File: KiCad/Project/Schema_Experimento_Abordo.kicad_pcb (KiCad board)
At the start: 2 copper layers, 58 x 58 mm, 29 parts, among them SW1 RESET, U1 ESP32-S3-WROOM-1, U2 BME280, U5 Micro_SD, U6 ZC323200, U7 SGP30, U9 AP2112K-3.3

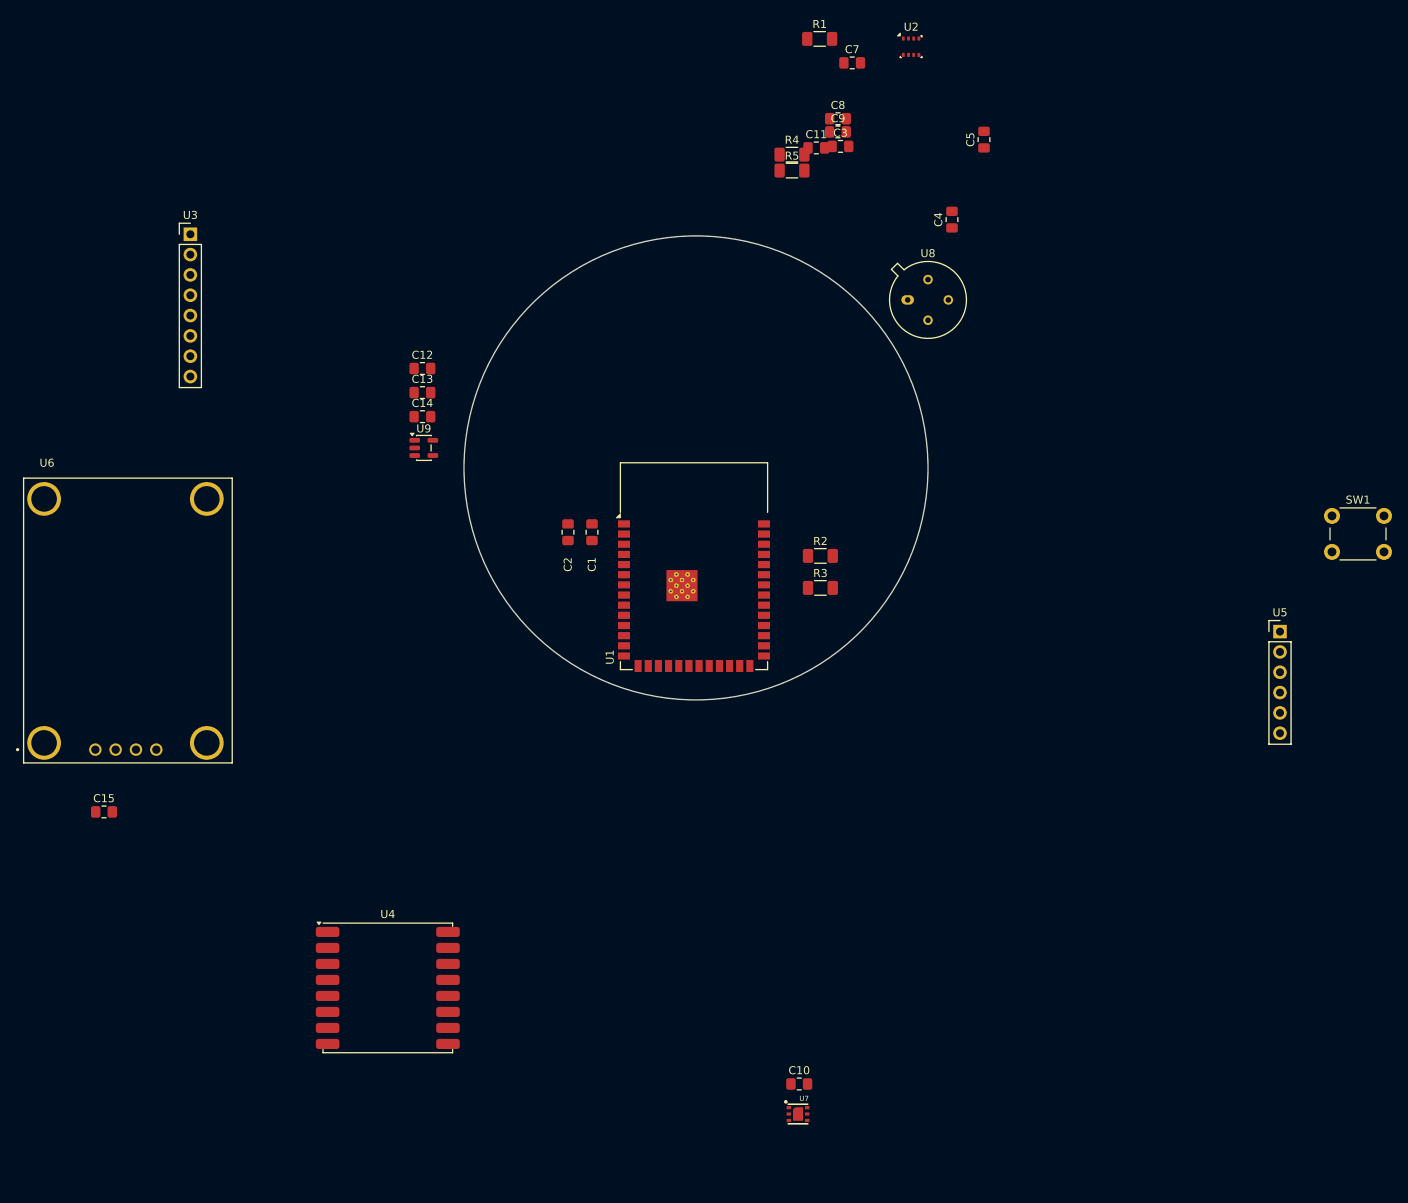
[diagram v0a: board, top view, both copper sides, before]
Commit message: Esquematico limpio y probado. PCB Actualizado. Falta definir si se cambia el U9 por un Buck-boost
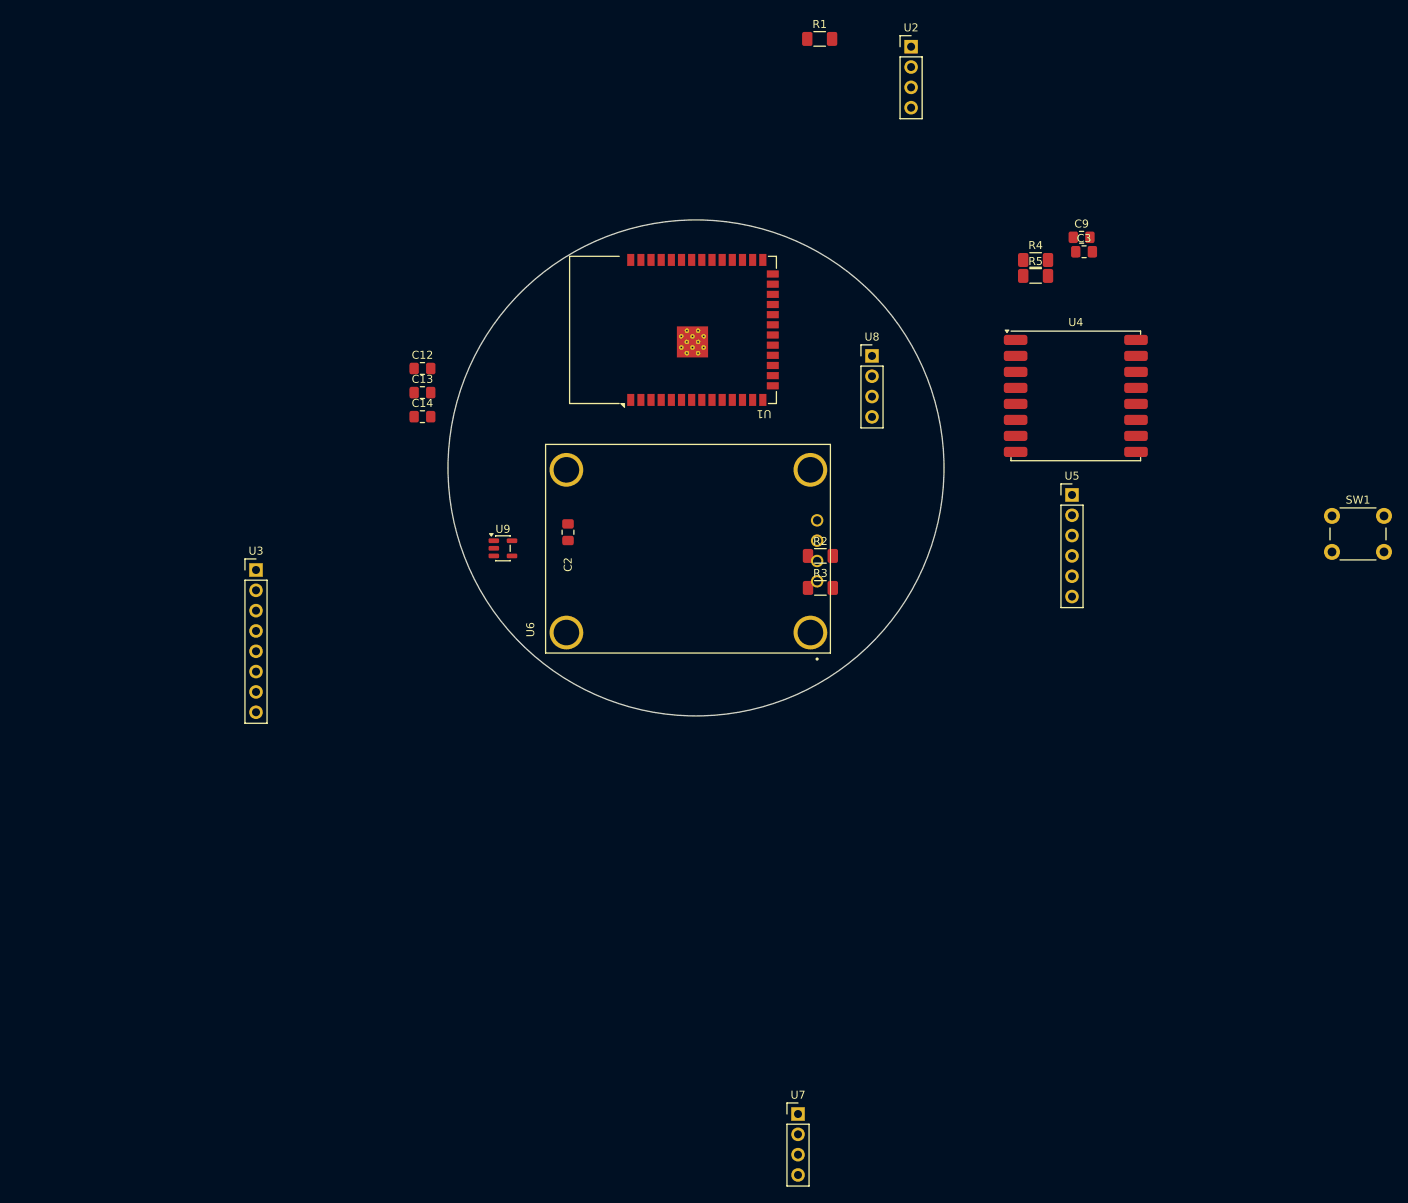
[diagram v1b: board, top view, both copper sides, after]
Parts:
- removed C1: 0.1uF, Capacitor_SMD:C_0805_2012Metric_Pad1.18x1.45mm_HandSolder
- removed C10, C11, C15, C4, C5, C7, C8: 100nF, Capacitor_SMD:C_0805_2012Metric_Pad1.18x1.45mm_HandSolder
- U2: footprint Package_LGA:Bosch_LGA-8_2.5x2.5mm_P0.65mm_ClockwisePinNumbering -> Connector_PinHeader_2.54mm:PinHeader_1x04_P2.54mm_Vertical
- U7: footprint SGP30:SGP30 -> Connector_PinHeader_2.54mm:PinHeader_1x04_P2.54mm_Vertical
- U8: footprint Package_TO_SOT_THT:TO-39-4 -> Connector_PinHeader_2.54mm:PinHeader_1x04_P2.54mm_Vertical
- moved U4 113.5 mm to (147.5, 91.0)
- moved U6 70.5 mm to (99.0, 110.0), turned to 90 degrees
- moved U3 42.8 mm to (45.0, 112.8)
- moved C3 33.2 mm to (148.5, 73.0)
- moved C9 33.2 mm to (148.2, 71.2)
- moved R4 33.2 mm to (142.4, 74.0)
- moved R5 33.2 mm to (142.4, 76.0)
- moved U5 31.1 mm to (147.0, 103.4)
- moved U1 29.6 mm to (97.1, 82.8), turned to 90 degrees
- moved U9 16.0 mm to (75.9, 110.0)
- moved U8 8.30 mm to (122.0, 86.0)
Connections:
- R2 pad 1: /SDA I2C -> /SDA
- R3 pad 1: /SCL I2C -> /SCL
- U1 pad 24: /SDA I2C -> /SDA
- U1 pad 25: /SCL I2C -> /SCL
- U1 pad 40: Net-(U1-GND-Pad40) -> GND
- U1 pad 41: Net-(U1-GND-Pad40) -> GND
- U2 pad 3: /D32 -> /SCL
- U2 pad 4: /D33 -> /SDA
- U3 pad 3: /D32 -> /SCL
- U3 pad 4: /D33 -> /SDA
- U3 pad 7: (no net) -> GND
- U3 pad 8: /D27 -> /MPU6050 INT
- U4 pad 11: /D26 -> /DIO0 LoRa
- U4 pad 2: /D19 -> /MISO SPI
- U4 pad 3: /D23 -> /MOSI SPI
- U4 pad 4: /D18 -> /SCK SPI
- U4 pad 5: /D5 -> /NSS LoRa
- U4 pad 6: /D14 -> /RST LoRa
- U5 pad 2: /D13 -> /CS MicroSD
- U5 pad 3: /D23 -> /MOSI SPI
- U5 pad 4: /D18 -> /SCK SPI
- U5 pad 5: /D19 -> /MISO SPI
- U6 pad 2: /RX2 -> /GPS_RX
- U6 pad 3: /TX2 -> /GPS_TX
- U6 pad SH1: Net-(U6-SHIELD-PadSH1) -> GND
- U6 pad SH2: Net-(U6-SHIELD-PadSH1) -> GND
- U6 pad SH3: Net-(U6-SHIELD-PadSH1) -> GND
- U6 pad SH4: Net-(U6-SHIELD-PadSH1) -> GND
- U7 pad 3: /D33 -> /SCL
- U7 pad 4: GND -> /SDA
- U8 pad 3: /D32 -> /SCL
- U8 pad 4: /D33 -> /SDA
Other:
- board size 58 x 58 mm -> 62 x 62 mm
